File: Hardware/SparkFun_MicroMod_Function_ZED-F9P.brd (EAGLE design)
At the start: 38 x 65 mm, 112 parts, among them J10 QWIIC_RA, J11 Bus Selection, J12 USB Female Type C Connector, J2 MICROMOD_STANDARD, J3 QWIIC_RA, J4 U.FL, J5 455-1750-1-ND, J8 Bus Selection, Q1 DMP21D0UT, U1 EEPROM, U10 OPA344, U11 74LVC4066D_QUAD_BILATERAL_SWI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, U12 74LVC4066D_QUAD_BILATERAL_SWI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, U2 U-BLOX_ZED-F9P, U3 FIN1017MXSOIC-8, U4 SN74AUP1T04DCK, U5 SN74LVC1G66DRYR, U6 74LVC541ABQ, U7 3.3V, U9 SN74AUP1T04DCK

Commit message: First day of layout.
Laid out most of the board with airwires. Have a rough idea of grounding so far so good. Have had to replace a fair bit of components for smaller ones. Those 0603's look massive on such a small board.
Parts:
- removed C17, C19, C20: 0.1uF, SparkFun-Capacitors:0603
- removed C18: 2.2uF, SparkFun-Capacitors:0402-TIGHT
- removed D11: RED, SparkFun-LED:LED-0603
- removed D13: PESD0402, SparkFun-DiscreteSemi:0402
- removed D9: 3A/10V/280mV, SparkFun-DiscreteSemi:SOD-323
- removed JP13: JUMPER-SMT_2_NO_SILK, SparkFun-Jumpers:SMT-JUMPER_2_NO_SILK
- removed JP9: JUMPER-SMT_2_NC_TRACE_SILK, SparkFun-Jumpers:SMT-JUMPER_2_NC_TRACE_SILK
- removed R18, R24: 100k, SparkFun-Resistors:0603
- removed R20: 1k, SparkFun-Resistors:0603
- removed R23: 2.0k, SparkFun-Resistors:0603
- removed R27: 10, SparkFun-Resistors:0603
- removed SUPPLY35: 2PT_GND_TIE, SparkFun-PowerSymbols:2PT_GND_TIE
- removed TP20: TEST-POINT3, SparkFun-Connectors:PAD.03X.03
- removed U12: 74LVC4066D_QUAD_BILATERAL_SWITCH, SparkFun-IC-Logic:SO14
- added C16, C4, C6: 0.1uF, SparkFun-Capacitors:0402-TIGHT
- added C5: 10nF, SparkFun-Capacitors:0402-TIGHT
- added D2: 3A/10V/280mV, SparkFun-DiscreteSemi:SOD-323
- added D5: RED, SparkFun-LED:LED-0603
- added D8: PESD0402-0402T, SparkFun-DiscreteSemi:0402-TIGHT
- added JP3: JUMPER-SMT_2_NO_SILK, SparkFun-Jumpers:SMT-JUMPER_2_NO_SILK
- added JP6: JUMPER-SMT_2_NC_TRACE_SILK, SparkFun-Jumpers:SMT-JUMPER_2_NC_TRACE_SILK
- added R13, R16: 100k, SparkFun-Resistors:0603
- added R14: 10, SparkFun-Resistors:0603
- added R15: 68.1k, SparkFun-Resistors:0603
- added R17: 10k, SparkFun-Resistors:0603
- added SUPPLYTIE1: 2PT_GND_TIE, SparkFun-PowerSymbols:2PT_GND_TIE
- added TP11: TEST-POINT3, SparkFun-Connectors:PAD.03X.03
- added U8: U-BLOX_ZED-F9P, MicroMod_Function_GNSS_ublox_ZED_F9P:ZED-F9P
- C1, C2, C3, C9: device SparkFun-Capacitors:0603 -> SparkFun-Capacitors:0402-TIGHT
- C10, C14: device SparkFun-Capacitors:0402 -> SparkFun-Capacitors:0402-TIGHT
- C11: value 0.1uF -> 2.2uF; device SparkFun-Capacitors:0603 -> SparkFun-Capacitors:0402-TIGHT
- C12: value 0.1uF -> 1.0uF; device SparkFun-Capacitors:0402 -> SparkFun-Capacitors:0402-TIGHT
- C13: value 10nF -> 0.1uF
- C15: value CBR04C470J5GAC -> 0.1uF; device MicroMod_Function_GNSS_ublox_ZED_F9P:0402-TIGHT -> SparkFun-Capacitors:0402-TIGHT
- C7: value 1.0uF -> 0.1uF; device SparkFun-Capacitors:0603 -> SparkFun-Capacitors:0402-TIGHT
- C8: value 0.1uF -> CBR04C470J5GAC; device SparkFun-Capacitors:0402-TIGHT -> MicroMod_Function_GNSS_ublox_ZED_F9P:0402-TIGHT
- D3: value BLUE -> PRTR5V0U2F; device SparkFun-LED:LED-0603 -> SparkFun-IC-Power:SOT886
- D4: value BLUE -> 0.5A/40V/420mV; device SparkFun-LED:LED-0603 -> SparkFun-DiscreteSemi:SOD-323
- D6: value PRTR5V0U2F -> BLUE; device SparkFun-IC-Power:SOT886 -> SparkFun-LED:LED-0603
- D7: value 0.5A/40V/420mV -> BLUE; device SparkFun-DiscreteSemi:SOD-323 -> SparkFun-LED:LED-0603
- J1: value (none) -> USB Female Type C Connector; device SparkFun-Connectors:1X01 -> SparkFun-Connectors:USB-C-16P-4LAYER-ISOLATED
- J10: value QWIIC_RA -> U.FL; device SparkFun-Connectors:JST04_1MM_RA -> SparkFun-Connectors:U.FL
- J11: value Bus Selection -> 455-1750-1-ND; device SparkFun-Connectors:1X03_LOCK -> SparkFun-Connectors:1X03
- J12: value USB Female Type C Connector -> (none); device SparkFun-Connectors:USB-C-16P-4LAYER-ISOLATED -> SparkFun-Connectors:1X01
- J13, J14: device SparkFun-Connectors:1X01 -> SparkFun-Connectors:1X02
- J15, J16: value (none) -> QWIIC_RA; device SparkFun-Connectors:1X01 -> SparkFun-Connectors:JST04_1MM_RA
- J17: device SparkFun-Connectors:1X01 -> SparkFun-Connectors:1X04
- J18: value (none) -> Bus Selection; device SparkFun-Connectors:1X02 -> SparkFun-Connectors:1X03_LOCK
- J3: value QWIIC_RA -> Bus Selection; device SparkFun-Connectors:JST04_1MM_RA -> SparkFun-Connectors:1X03_LOCK
- J4: value U.FL -> (none); device SparkFun-Connectors:U.FL -> SparkFun-Connectors:1X01
- J5: value 455-1750-1-ND -> (none); device SparkFun-Connectors:1X03 -> SparkFun-Connectors:1X01
- J6: device SparkFun-Connectors:1X04 -> SparkFun-Connectors:1X01
- J8: value Bus Selection -> (none); device SparkFun-Connectors:1X03_LOCK -> SparkFun-Connectors:1X01
- J9: device SparkFun-Connectors:1X02 -> SparkFun-Connectors:1X01
- R10: value 27 -> 10k; device SparkFun-Resistors:0402-TIGHT -> SparkFun-Resistors:0603
- R11: value 3.3k -> 10k
- R12: value 68.1k -> 1k
- R3: value 10k -> 5.1k
- R4: value 10k -> 3.3k
- R5, R6: value 1k -> 27; device SparkFun-Resistors:0603 -> SparkFun-Resistors:0402-TIGHT
- R7: value 10k -> 1k
- R8: value 5.1k -> 1k
- R9: value 27 -> 1k; device SparkFun-Resistors:0402-TIGHT -> SparkFun-Resistors:0603
- U1: value EEPROM -> SN74LVC1G66DRYR; device SparkFun-IC-Memory:SO08 -> MicroMod_Function_GNSS_ublox_ZED_F9P:USON_DRY0006A
- U10: value OPA344 -> SN74AUP1T04DCK; device SparkFun-IC-Amplifiers:SOT23-5 -> MicroMod_Function_GNSS_ublox_ZED_F9P:SC-70-5_DCK
- U11: value 74LVC4066D_QUAD_BILATERAL_SWITCH -> SN74AUP1T04DCK; device SparkFun-IC-Logic:SO14 -> MicroMod_Function_GNSS_ublox_ZED_F9P:SC-70-5_DCK
- U2: value U-BLOX_ZED-F9P -> 3.3V; device MicroMod_Function_GNSS_ublox_ZED_F9P:ZED-F9P -> SparkFun-IC-Power:SOT23-5
- U3: value FIN1017MXSOIC-8 -> EEPROM; device MicroMod_Function_GNSS_ublox_ZED_F9P:SO08 -> SparkFun-IC-Memory:SO08
- U4: value SN74AUP1T04DCK -> 74LVC4066D_QUAD_BILATERAL_SWITCH; device MicroMod_Function_GNSS_ublox_ZED_F9P:SC-70-5_DCK -> SparkFun-IC-Logic:SO14
- U5: value SN74LVC1G66DRYR -> 74LVC4066D_QUAD_BILATERAL_SWITCH; device MicroMod_Function_GNSS_ublox_ZED_F9P:USON_DRY0006A -> SparkFun-IC-Logic:SO14
- U6: value 74LVC541ABQ -> OPA344; device MicroMod_Function_GNSS_ublox_ZED_F9P:DHVQFN20 -> SparkFun-IC-Amplifiers:SOT23-5
- U7: value 3.3V -> 74LVC541ABQ; device SparkFun-IC-Power:SOT23-5 -> MicroMod_Function_GNSS_ublox_ZED_F9P:DHVQFN20
- U9: value SN74AUP1T04DCK -> FIN1017MXSOIC-8; device MicroMod_Function_GNSS_ublox_ZED_F9P:SC-70-5_DCK -> MicroMod_Function_GNSS_ublox_ZED_F9P:SO08
- moved J1 241.5 mm to (30.7, 58.9), turned to 180 degrees
- moved J18 238.4 mm to (1.60, 37.1), turned to 270 degrees
- moved TP19 237.5 mm to (40.4, 39.2), flipped to the bottom
- moved TP10 235.5 mm to (28.5, 23.7), flipped to the bottom
- moved TP2 227.8 mm to (22.5, 27.7), flipped to the bottom
- moved TP6 226.3 mm to (30.9, 23.8), flipped to the bottom
- moved J14 225.8 mm to (34.0, 39.2)
- moved R12 225.5 mm to (14.2, 54.9), turned to 180 degrees
- moved J13 221.8 mm to (34.0, 36.3)
- moved J12 220.3 mm to (28.5, 45.5)
- moved TP1 220.3 mm to (13.6, 32.6), flipped to the bottom
- moved TP7 219.9 mm to (20.9, 17.7), flipped to the bottom
- moved TP8 219.6 mm to (22.2, 17.7), flipped to the bottom
- moved J15 215.1 mm to (40.8, 23.8), turned to 90 degrees
- moved J16 214.5 mm to (53.7, 15.2), turned to 270 degrees
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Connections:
- removed net !SAFEBOOT!: J7.1, TP12.1
- removed net ANT_!SHORT!: C13.1, L1.P$1, R27.2, U10.4
- removed net ANT_DETECT: U10.1
- removed net ANT_OFF: J11.2, Q1.P$3
- removed net VDD: C1.1, J1.1, R3.2, TP3.1, U7.5
- new net N$14: C10.1, C9.1, R15.2, R16.2, U8.38
- net !RESET!: now also J13.1, TP18.1, U7.P$3; no longer J18.1, TP14.1, U6.P$3
- net !ZED_DSEL!: now also U11.P$4, U5.12, U5.13, U5.5, U5.6; no longer U12.12, U12.13, U12.5, U12.6, U9.P$4
- net 3.3V: now also C14.1, D4.A, J15.2, J16.2, U3.8, U9.1; no longer C12.1, D7.A, J10.2, J3.2, U1.8, U3.1
- net 5V: now also C1.1, D2.C, U2.1; no longer C3.1, D9.C, U5.P$4, U5.P$6, U7.1
- net A0: now also U3.1; no longer U1.1
- net A1: now also U3.2; no longer U1.2
- net A2: now also U3.3; no longer U1.3
- net EWP: now also JP2.2, U3.7; no longer JP1.2, U1.7
- net EXTINT: now also J14.1, TP19.1, U7.P$4; no longer J9.1, TP10.1, U6.P$4
- net GEO_STAT: now also U7.P$11; no longer U6.P$11
- net GND: now also C14.2, D3.2, J1.GND, J1.GND2, J11.3, J13.2, J14.2, J15.1, J16.1, J17.1, J17.4, J5.1, JP2.1, JP3.2, JP4.2, JP6.1, R3.1, SUPPLYTIE1.P$2, TP2.1, U1.P$3, U2.2, U9.4; no longer C12.2, D6.2, J10.1, J12.GND, J12.GND2, J13.1, J14.1, J18.2, J3.1, J5.3, J6.4, J9.2, JP1.1, JP13.2, JP4.1, JP9.2, R8.1, SUPPLY35.P$2, TP1.1, U1.4, U5.P$3, U7.2
- net GND_RF: now also C11.2, C12.2, C15.2, C16.2, C4.2, C5.2, C6.2, D8.2, J10.1, J10.2, J18.3, J8.1, J9.1, R11.1, R13.1, R16.1, SUPPLYTIE1.P$1, U10.P$3, U11.P$3, U4.7, U5.7, U6.2, U7.P$10, U7.P$21, U8.1, U8.100, U8.101, U8.102, U8.12, U8.14, U8.3, U8.32, U8.37, U8.41, U8.48, U8.55, U8.56, U8.57, U8.58, U8.59, U8.60, U8.61, U8.62, U8.63, U8.64, U8.65, U8.66, U8.67, U8.68, U8.69, U8.70, U8.71, U8.72, U8.73, U8.74, U8.75, U8.76, U8.77, U8.78, U8.79, U8.80, U8.81, U8.82, U8.83, U8.84, U8.85, U8.86, U8.87, U8.88, U8.89, U8.90, U8.91, U8.92, U8.93, U8.94, U8.95, U8.96, U8.97, U8.98, U8.99; no longer C11.1, C14.1, C17.1, C18.2, C19.2, C20.2, C8.2, D13.2, J15.1, J16.1, J4.1, J4.2, J8.3, R18.1, R24.1, R7.1, SUPPLY35.P$1, U10.2, U11.7, U12.7, U2.1, U2.100, U2.101, U2.102, U2.12, U2.14, U2.3, U2.32, U2.37, U2.41, U2.48, U2.55, U2.56, U2.57, U2.58, U2.59, U2.60, U2.61, U2.62, U2.63, U2.64, U2.65, U2.66, U2.67, U2.68, U2.69, U2.70, U2.71, U2.72, U2.73, U2.74, U2.75, U2.76, U2.77, U2.78, U2.79, U2.80, U2.81, U2.82, U2.83, U2.84, U2.85, U2.86, U2.87, U2.88, U2.89, U2.90, U2.91, U2.92, U2.93, U2.94, U2.95, U2.96, U2.97, U2.98, U2.99, U4.P$3, U6.P$10, U6.P$21, U9.P$3
- net IO_!OE!: now also U10.P$4, U7.P$1, U7.P$19; no longer U4.P$4, U6.P$1, U6.P$19
- net MM_!CS!: now also TP11.1, U5.2; no longer TP8.1, U12.2
- net MM_CIPO: now also TP13.1, U5.9; no longer TP6.1, U12.9
- net MM_COPI: now also TP12.1, U5.10; no longer TP2.1, U12.10
- net MM_RX: now also TP7.1, U4.10; no longer TP15.1, U11.10
- net MM_SCK: now also TP10.1, U5.3; no longer TP7.1, U12.3
- net MM_SCL: now also J15.4, J16.4, TP5.1, U3.6, U4.3; no longer J10.4, J3.4, TP19.1, U1.6, U11.3
- net MM_SDA: now also J15.3, J16.3, TP6.1, U3.5, U4.2; no longer J10.3, J3.3, TP20.1, U1.5, U11.2
- net MM_TX: now also TP8.1, U4.9; no longer TP16.1, U11.9
- net N$1: now also D3.3, J1.A6, J1.B6; no longer D6.1, J12.A6, J12.B6
- net N$10: now also J18.1, R17.1; no longer J8.1, R3.1
- net N$11: now also J3.1, R10.1; no longer J11.1, R4.1
- net N$12: now also J3.3, R11.2; no longer J11.3, R7.2
- net N$13: now also R12.1, R14.1; no longer R23.2, R27.1
- net N$16: now also D2.A, JP1.2; no longer D1.A, JP2.2
- net N$2: now also D3.1, J1.A7, J1.B7; no longer D6.3, J12.A7, J12.B7
- net N$26: now also JP4.1, R7.1; no longer JP9.1, R20.1
- net N$27: now also JP5.2, R8.1; no longer JP4.2, R5.1
- net N$28: now also D6.C, R8.2; no longer D3.C, R5.2
- net N$29: now also D7.C, R9.2; no longer D4.C, R6.2
- net N$3: now also J1.B5; no longer J12.B5
- net N$30: now also D5.C, R7.2; no longer D11.C, R20.2
- net N$32: now also D4.C, R4.2; no longer D7.C, R11.2
- net N$4: now also J1.A5, R3.2; no longer J12.A5, R8.2
- net N$48: now also R12.2, R13.2, U6.3; no longer R23.1, R24.2, U10.3
- net N$5: now also D3.4, R5.1; no longer D6.6, R9.1
- net N$51: now also J17.3, U9.8; no longer J6.3, U3.8
- net N$6: now also D3.6, R6.1; no longer D6.4, R10.1
- net N$7: now also C8.1, D8.1, J10.FEED; no longer C15.1, D13.1, J4.FEED
- net N$8: now also JP6.2, R9.1; no longer JP5.2, R6.1
- net N$9: now also J17.2, U9.7; no longer J6.2, U3.7
- net PPS: now also D6.A, TP9.1, U7.P$18, U9.2; no longer D3.A, TP13.1, U3.2, U6.P$18
- net PWR_EN: now also U2.3; no longer U7.3
- net RF_IN: now also C8.2, U8.2; no longer C15.2, U2.2
- net RTK_STAT: now also D7.A, U7.P$12; no longer D4.A, U6.P$12
- net RX2/RTCM: now also J11.1, TP15.1, U7.P$7; no longer J5.1, TP17.1, U6.P$7
- net SHLD: now also J1.SHLD1, J1.SHLD2, J1.SHLD3, J1.SHLD4, J1.SHLD5, J1.SHLD6, J1.SHLD7, J1.SHLD8, JP3.1; no longer J12.SHLD1, J12.SHLD2, J12.SHLD3, J12.SHLD4, J12.SHLD5, J12.SHLD6, J12.SHLD7, J12.SHLD8, JP13.1
- net TX2/RTCM: now also J11.2, TP16.1, U7.P$14; no longer J5.2, TP18.1, U6.P$14
- net TX_READY: now also TP14.1, U7.P$15; no longer TP9.1, U6.P$15
- net VIN: now also D1.A; no longer D9.A
- net V_BATT: now also C11.1, J7.1, R4.1, TP3.1, U8.36; no longer C18.1, J17.1, R11.1, TP5.1, U2.36
- net V_RF: now also R10.2, U8.7; no longer R4.2, U2.7
- net V_USB: now also D3.5, J1.VBUS1, J1.VBUS2, JP1.1, U1.P$1; no longer D6.5, J12.VBUS1, J12.VBUS2, JP2.1, U5.P$1
- net V_ZED: now also C12.1, C13.1, C15.1, C16.1, C3.1, C4.1, C6.1, C7.1, D5.A, J4.1, R17.2, TP1.1, U1.P$4, U1.P$6, U10.P$2, U10.P$5, U11.P$5, U2.5, U4.14, U5.14, U6.5, U7.P$20, U8.33, U8.34; no longer C10.1, C11.2, C14.2, C17.2, C19.1, C20.1, C9.1, D11.A, U10.5, U11.14, U12.14, U2.33, U2.34, U4.P$2, U4.P$5, U6.P$20, U9.P$5
- net ZED_!RESET!: now also U7.P$17, U8.49; no longer U2.49, U6.P$17
- net ZED_!SAFEBOOT!: now also J12.1, TP17.1, U8.50; no longer U2.50
- net ZED_ANT_!SHORT!: now also C5.1, L1.P$1, R14.2, U6.4, U8.6; no longer U2.6
- net ZED_ANT_DETECT: now also U6.1, U8.4; no longer U2.4
- net ZED_ANT_OFF: now also J3.2, Q1.P$3, U8.5; no longer U2.5
- net ZED_DSEL: now also J18.2, U11.P$2, U4.12, U4.13, U4.5, U4.6, U8.47; no longer J8.2, U11.12, U11.13, U11.5, U11.6, U2.47, U9.P$2
- net ZED_EXTINT: now also U7.P$16, U8.51; no longer U2.51, U6.P$16
- net ZED_GEO_STAT: now also U7.P$9, U8.19; no longer U2.19, U6.P$9
- net ZED_PPS: now also U7.P$2, U8.53; no longer U2.53, U6.P$2
- net ZED_RTK_STAT: now also U7.P$8, U8.20; no longer U2.20, U6.P$8
- net ZED_RX/COPI: now also U4.11, U5.11, U8.43; no longer U11.11, U12.11, U2.43
- net ZED_RX2/RTCM: now also U7.P$13, U8.26; no longer U2.26, U6.P$13
- net ZED_SCL/SCK: now also U4.4, U5.4, U8.45; no longer U11.4, U12.4, U2.45
- net ZED_SDA/!CS!: now also U4.1, U5.1, U8.44; no longer U11.1, U12.1, U2.44
- net ZED_TX/CIPO: now also U4.8, U5.8, U8.42; no longer U11.8, U12.8, U2.42
- net ZED_TX2/RTCM: now also U7.P$6, U8.27; no longer U2.27, U6.P$6
- net ZED_TX_READY: now also U7.P$5, U8.46; no longer U2.46, U6.P$5
- net ZED_USB_DET: now also R15.1, U1.P$2; no longer C7.1, C8.1, R12.1, R12.2, R18.2, U2.38, U5.P$2
- net ZED_USB_N: now also R6.2, U8.39; no longer R10.2, U2.39
- net ZED_USB_P: now also R5.2, U8.40; no longer R9.2, U2.40
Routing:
- added copper zone on layer 2, net GND
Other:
- outline, holes or cut-outs redrawn

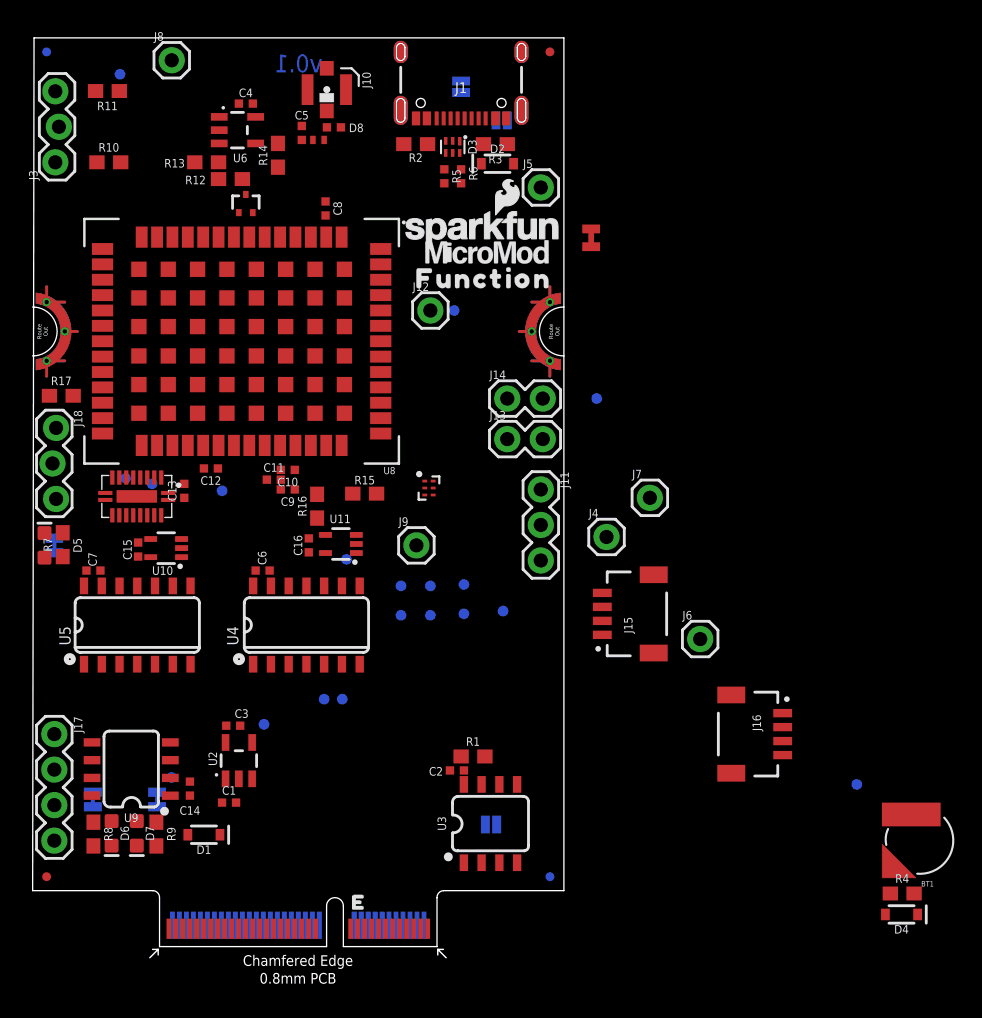
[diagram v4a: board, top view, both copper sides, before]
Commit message: Everything tentatively placed on board.
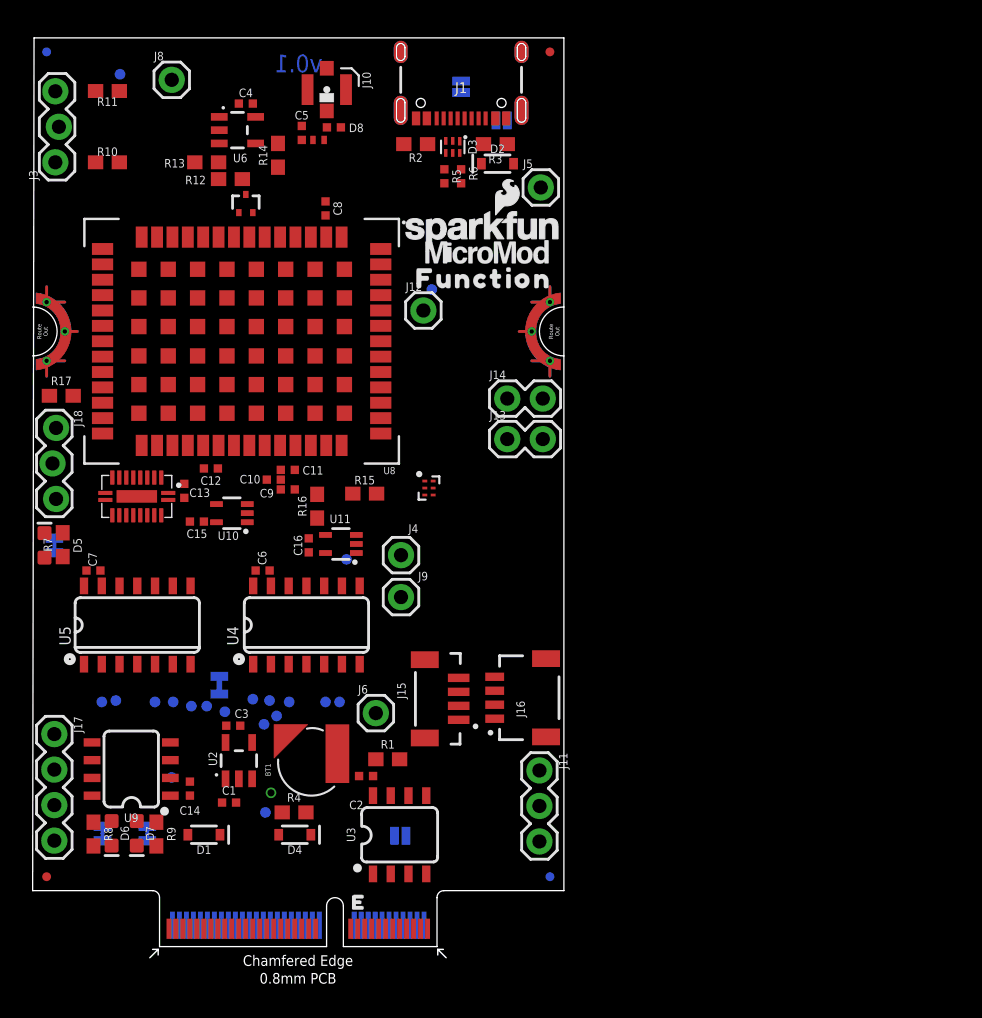
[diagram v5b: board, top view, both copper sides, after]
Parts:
- J15: value QWIIC_RA -> QWIIC_VERT; device SparkFun-Connectors:JST04_1MM_RA -> SparkFun-Connectors:JST04_1MM_VERT
- J7: device SparkFun-Connectors:1X01 -> SparkFun-Connectors:1X01_SMALL
- moved R4 43.9 mm to (18.8, 9.60)
- moved BT1 43.9 mm to (20.0, 13.2), turned to 90 degrees
- moved D4 43.8 mm to (18.8, 8.00)
- moved TP3 42.3 mm to (16.7, 9.60)
- moved SUPPLYTIE1 41.6 mm to (13.4, 18.7), flipped to the bottom
- moved J7 34.3 mm to (17.1, 11.0)
- moved TP19 32.7 mm to (15.8, 17.7)
- moved J6 23.8 mm to (24.6, 16.7)
- moved TP10 23.3 mm to (6.00, 17.6)
- moved TP11 22.3 mm to (5.00, 17.5)
- moved TP16 22.3 mm to (12.5, 17.2)
- moved TP12 21.4 mm to (8.80, 17.5)
- moved J16 20.8 mm to (33.1, 17.8), turned to 90 degrees
- moved J11 20.1 mm to (36.3, 12.6)
- moved TP18 18.8 mm to (17.5, 16.5)
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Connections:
- net GND: no longer JP4.2
- net GND_RF: now also JP4.2
- net V_BATT: now also J7.P$1; no longer J7.1

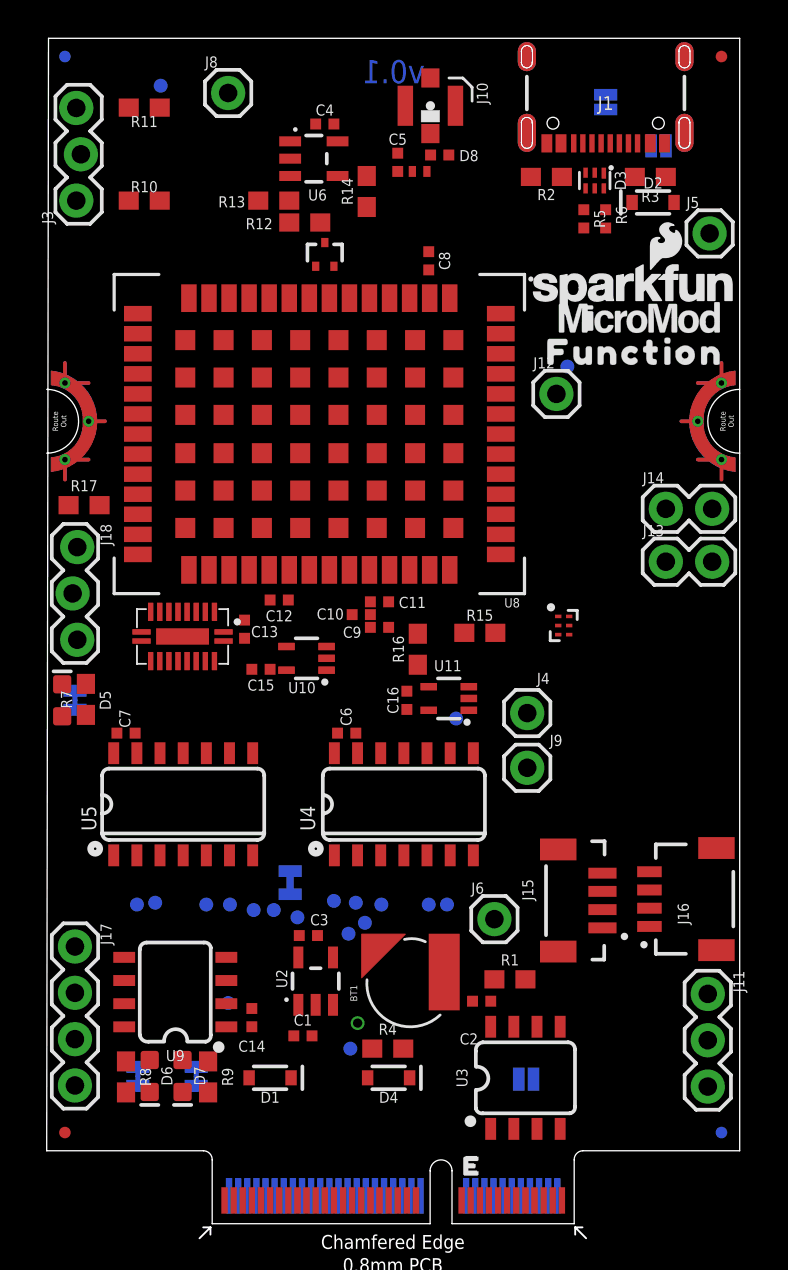
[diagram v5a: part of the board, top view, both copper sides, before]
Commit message: 1st draft power planes.
Added split power planes to layout on inner layers.
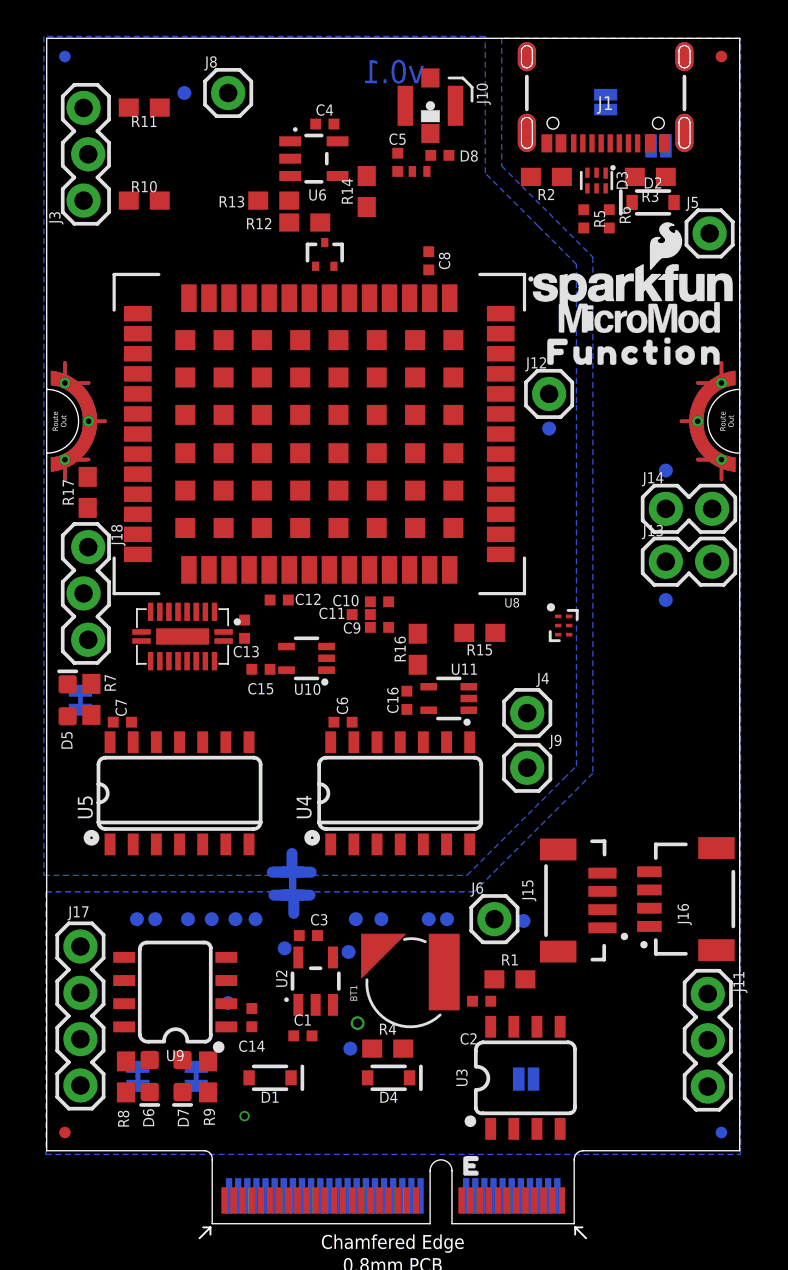
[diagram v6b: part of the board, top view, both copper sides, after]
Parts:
- moved TP19 29.8 mm to (34.0, 41.3)
- moved TP18 24.2 mm to (34.0, 34.2)
- moved TP2 11.7 mm to (26.2, 16.6)
- moved TP17 3.54 mm to (27.6, 43.6)
- moved TP1 1.84 mm to (13.1, 15.1)
- moved TP4 1.36 mm to (7.60, 62.0)
- moved TP12 1.28 mm to (7.80, 16.7)
- moved TP13 1.28 mm to (9.10, 16.7)
- moved TP15 1.12 mm to (10.4, 16.7)
- moved TP16 1.12 mm to (11.5, 16.7)
- moved TP14 1.00 mm to (16.6, 14.9)
- moved TP10 0.90 mm to (6.00, 16.7)
- moved TP6 0.90 mm to (17.0, 16.7)
- moved TP11 0.80 mm to (5.00, 16.7)
- moved TP5 0.80 mm to (18.4, 16.7)
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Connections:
- net N$51 renamed PPS_DIFF_N
- net N$9 renamed PPS_DIFF_P
- net GND: no longer U1.P$3
- net GND_RF: now also U1.P$3
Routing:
- net GND: track 0.00 -> 5.40 mm
- net GND_RF: track 0.00 -> 3.14 mm
- added copper zone on layer 15, net 3.3V
- added copper zone on layer 16, net GND
- added copper zone on layer 16, net GND_RF
- added copper zone on layer 2, net GND_RF
- added copper zone on layer 15, net V_ZED
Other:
- outline, holes or cut-outs redrawn

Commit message: Board updates from time off.
Airport board layout was time well spent.
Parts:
- moved D5 35.3 mm to (10.1, 62.9), turned to 0 degrees
- moved J4 34.9 mm to (2.20, 53.1)
- moved JP4 34.5 mm to (10.1, 62.2), turned to 0 degrees
- moved R7 33.7 mm to (10.2, 61.6), turned to 0 degrees
- moved J8 33.2 mm to (4.00, 29.3)
- moved J9 29.4 mm to (24.0, 54.3)
- moved R17 27.6 mm to (27.6, 29.1)
- moved J18 24.4 mm to (25.5, 30.0)
- moved TP1 9.92 mm to (15.6, 24.7)
- moved TP2 2.15 mm to (25.4, 14.6)
- moved TP5 1.42 mm to (17.5, 15.6)
- moved TP6 1.08 mm to (16.1, 16.1)
- moved U1 0.80 mm to (27.3, 33.3)
- moved C16 0.71 mm to (19.4, 28.1), turned to 180 degrees
- moved TP9 0.67 mm to (9.70, 11.5)
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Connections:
- net N$1 renamed USBC_P
- net N$2 renamed USBC_N
- net N$5 renamed USB_P
- net N$6 renamed USB_N
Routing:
- net ZED_SDA/!CS!: track 0.00 -> 40.4 mm, vias 0 -> 3
- net ZED_DSEL: track 0.00 -> 40.1 mm, vias 0 -> 6
- net ZED_RX/COPI: track 0.00 -> 39.4 mm, vias 0 -> 3
- net ZED_SCL/SCK: track 0.00 -> 38.0 mm, vias 0 -> 3
- net PPS: track 0.00 -> 34.4 mm, vias 0 -> 2
- net ZED_EXTINT: track 0.00 -> 33.9 mm, vias 0 -> 3
- net ZED_PPS: track 0.00 -> 32.1 mm, vias 0 -> 2
- net ZED_!RESET!: track 0.00 -> 31.3 mm, vias 0 -> 3
- net V_BATT: track 0.00 -> 28.4 mm, vias 0 -> 2
- net !ZED_DSEL!: track 0.00 -> 28.2 mm, vias 0 -> 6
- net ZED_TX/CIPO: track 0.00 -> 26.2 mm, vias 0 -> 3
- net ZED_TX_READY: track 0.00 -> 25.3 mm, vias 0 -> 3
- net ZED_ANT_OFF: track 0.00 -> 22.3 mm, vias 0 -> 2
- net V_ZED: track 0.00 -> 21.7 mm, vias 0 -> 13
- net SHLD: track 0.00 -> 20.7 mm
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- added copper zone on layer 1, net GND
- added copper zone on layer 1, net GND_RF
- added copper zone on layer 15, net V_USB
- added copper zone on layer 1, net V_ZED
